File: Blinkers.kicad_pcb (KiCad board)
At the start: 2 copper layers, 250 x 49 mm, 219 parts, among them J1 12V, J2 A1, J3 gnd, J4 A1, J5 A1, J6 A1, J7 A1, J8 A1, J9 brake, Q1 Q_NMOS_DGS, Q2 Q_NMOS_DGS, Q3 Q_NMOS_DGS, Q4 Q_NMOS_DGS, Q5 Q_NMOS_DGS, Q6 Q_NMOS_DGS

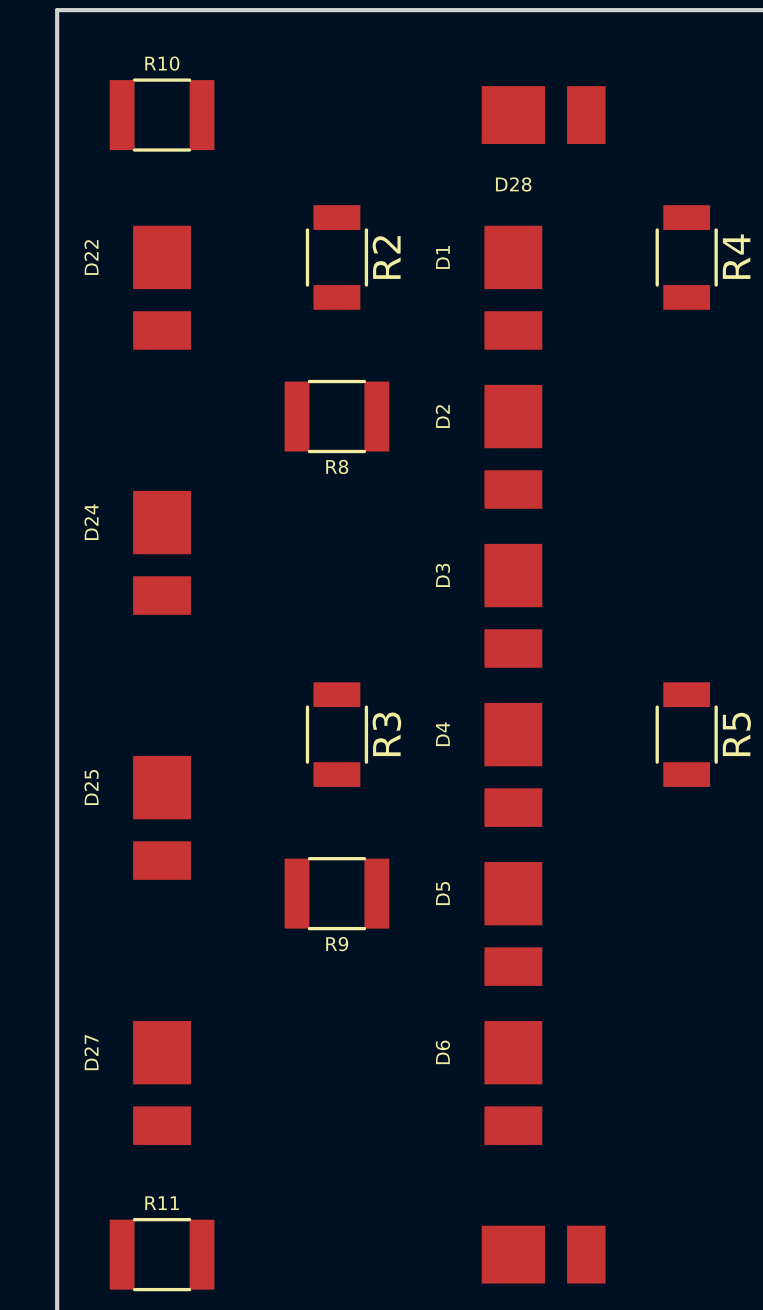
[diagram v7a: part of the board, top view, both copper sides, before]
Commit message: Fine-tuning WIP, rotating LEDs for closer connectons and moved VCC and GND.
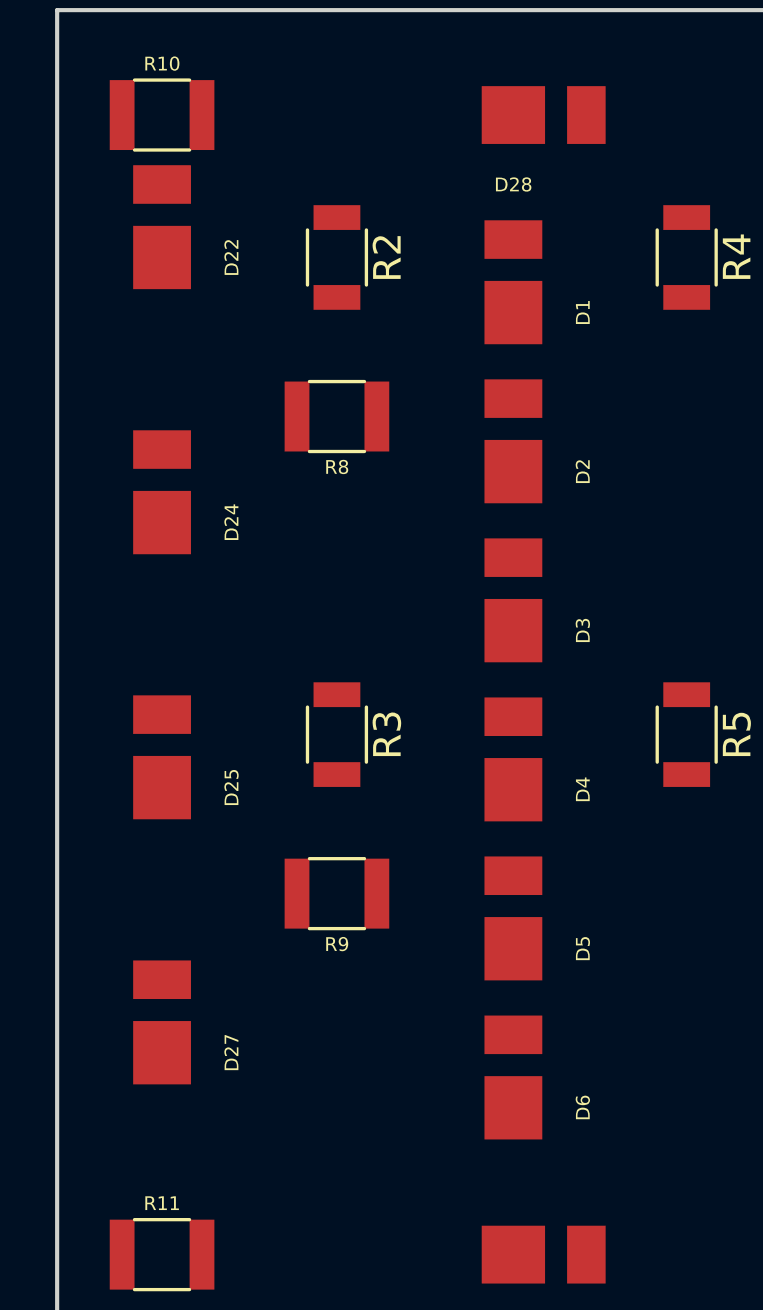
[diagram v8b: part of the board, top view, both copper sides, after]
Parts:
- moved D1 2.00 mm to (30.5, 92.3), turned to 90 degrees
- moved D2 2.00 mm to (30.5, 98.0), turned to 90 degrees
- moved D3 2.00 mm to (30.5, 103.8), turned to 90 degrees
- moved D4 2.00 mm to (30.5, 109.6), turned to 90 degrees
- moved D5 2.00 mm to (30.5, 115.4), turned to 90 degrees
- moved D6 2.00 mm to (30.5, 121.1), turned to 90 degrees
- turned D22 to 90 degrees
- turned D24 to 90 degrees
- turned D25 to 90 degrees
- turned D27 to 90 degrees
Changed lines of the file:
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@@
-(kicad_pcb (version 20171130) (host pcbnew 5.1.3-ffb9f22~84~ubuntu18.04.1)
+(kicad_pcb (version 20171130) (host pcbnew "(5.1.2)-2")
   (general
     (thickness 1.6)
@@
   )
   (module Footprints:D_2835 placed (layer F.Cu)
-    (at 17.78 90.2625 270)
+    (at 17.78 90.2625 90)
     (attr smd)
     (fp_text reference D22 (at 0 2.54 270) (layer F.SilkS)
@@
       (effects (font (size 0.5 0.5) (thickness 0.0625)))
     )
-    (pad 1 smd rect (at 0 0 270) (size 2.3 2.1) (layers F.Cu F.Paste F.Mask)
+    (pad 1 smd rect (at 0 0 90) (size 2.3 2.1) (layers F.Cu F.Paste F.Mask)
       (net 7 "Net-(D22-Pad1)"))
-    (pad 2 smd rect (at 2.65 0 270) (size 1.4 2.1) (layers F.Cu F.Paste F.Mask)
+    (pad 2 smd rect (at 2.65 0 90) (size 1.4 2.1) (layers F.Cu F.Paste F.Mask)
       (net 8 "Net-(D22-Pad2)"))
   )
   (module Footprints:D_2835 placed (layer F.Cu)
-    (at 17.78 99.8875 270)
+    (at 17.78 99.8875 90)
     (attr smd)
     (fp_text reference D24 (at 0 2.54 270) (layer F.SilkS)
@@
       (effects (font (size 0.5 0.5) (thickness 0.0625)))
     )
-    (pad 1 smd rect (at 0 0 270) (size 2.3 2.1) (layers F.Cu F.Paste F.Mask)
+    (pad 1 smd rect (at 0 0 90) (size 2.3 2.1) (layers F.Cu F.Paste F.Mask)
       (net 4 GND))
-    (pad 2 smd rect (at 2.65 0 270) (size 1.4 2.1) (layers F.Cu F.Paste F.Mask)
+    (pad 2 smd rect (at 2.65 0 90) (size 1.4 2.1) (layers F.Cu F.Paste F.Mask)
       (net 7 "Net-(D22-Pad1)"))
   )
   (module Footprints:D_2835 placed (layer F.Cu)
-    (at 17.78 109.512 270)
+    (at 17.78 109.512 90)
     (attr smd)
     (fp_text reference D25 (at 0 2.54 270) (layer F.SilkS)
@@
       (effects (font (size 0.5 0.5) (thickness 0.0625)))
     )
-    (pad 1 smd rect (at 0 0 270) (size 2.3 2.1) (layers F.Cu F.Paste F.Mask)
+    (pad 1 smd rect (at 0 0 90) (size 2.3 2.1) (layers F.Cu F.Paste F.Mask)
       (net 9 "Net-(D25-Pad1)"))
-    (pad 2 smd rect (at 2.65 0 270) (size 1.4 2.1) (layers F.Cu F.Paste F.Mask)
+    (pad 2 smd rect (at 2.65 0 90) (size 1.4 2.1) (layers F.Cu F.Paste F.Mask)
       (net 10 "Net-(D25-Pad2)"))
   )
   (module Footprints:D_2835 locked placed (layer F.Cu)
-    (at 17.78 119.138 270)
+    (at 17.78 119.138 90)
     (attr smd)
     (fp_text reference D27 (at 0 2.54 270) (layer F.SilkS)
@@
       (effects (font (size 0.5 0.5) (thickness 0.0625)))
     )
-    (pad 1 smd rect (at 0 0 270) (size 2.3 2.1) (layers F.Cu F.Paste F.Mask)
+    (pad 1 smd rect (at 0 0 90) (size 2.3 2.1) (layers F.Cu F.Paste F.Mask)
       (net 4 GND))
-    (pad 2 smd rect (at 2.65 0 270) (size 1.4 2.1) (layers F.Cu F.Paste F.Mask)
+    (pad 2 smd rect (at 2.65 0 90) (size 1.4 2.1) (layers F.Cu F.Paste F.Mask)
       (net 9 "Net-(D25-Pad1)"))
   )
@@
       (net 3 "Net-(D10-Pad1)"))
   )
-  (module Footprints:D_2835 locked placed (layer F.Cu)
-    (at 30.537 119.138 270)
+  (module Footprints:D_2835 placed (layer F.Cu)
+    (at 30.537 121.138 90)
     (attr smd)
     (fp_text reference D6 (at 0 2.54 270) (layer F.SilkS)
@@
       (effects (font (size 0.5 0.5) (thickness 0.0625)))
     )
-    (pad 1 smd rect (at 0 0 270) (size 2.3 2.1) (layers F.Cu F.Paste F.Mask)
+    (pad 1 smd rect (at 0 0 90) (size 2.3 2.1) (layers F.Cu F.Paste F.Mask)
       (net 3 "Net-(D10-Pad1)"))
-    (pad 2 smd rect (at 2.65 0 270) (size 1.4 2.1) (layers F.Cu F.Paste F.Mask)
+    (pad 2 smd rect (at 2.65 0 90) (size 1.4 2.1) (layers F.Cu F.Paste F.Mask)
       (net 64 "Net-(D5-Pad1)"))
   )
@@
       (net 70 "Net-(D12-Pad1)"))
   )
-  (module Footprints:D_2835 locked placed (layer F.Cu)
-    (at 30.537 113.362 270)
+  (module Footprints:D_2835 placed (layer F.Cu)
+    (at 30.537 115.362 90)
     (attr smd)
     (fp_text reference D5 (at 0 2.54 270) (layer F.SilkS)
@@
       (effects (font (size 0.5 0.5) (thickness 0.0625)))
     )
-    (pad 1 smd rect (at 0 0 270) (size 2.3 2.1) (layers F.Cu F.Paste F.Mask)
+    (pad 1 smd rect (at 0 0 90) (size 2.3 2.1) (layers F.Cu F.Paste F.Mask)
       (net 64 "Net-(D5-Pad1)"))
-    (pad 2 smd rect (at 2.65 0 270) (size 1.4 2.1) (layers F.Cu F.Paste F.Mask)
+    (pad 2 smd rect (at 2.65 0 90) (size 1.4 2.1) (layers F.Cu F.Paste F.Mask)
       (net 63 "Net-(D4-Pad1)"))
   )
@@
   )
   (module Footprints:D_2835 placed (layer F.Cu)
-    (at 30.537 107.588 270)
+    (at 30.537 109.588 90)
     (attr smd)
     (fp_text reference D4 (at 0 2.54 270) (layer F.SilkS)
@@
       (effects (font (size 0.5 0.5) (thickness 0.0625)))
     )
-    (pad 2 smd rect (at 2.65 0 270) (size 1.4 2.1) (layers F.Cu F.Paste F.Mask)
+    (pad 2 smd rect (at 2.65 0 90) (size 1.4 2.1) (layers F.Cu F.Paste F.Mask)
       (net 62 "Net-(D4-Pad2)"))
-    (pad 1 smd rect (at 0 0 270) (size 2.3 2.1) (layers F.Cu F.Paste F.Mask)
+    (pad 1 smd rect (at 0 0 90) (size 2.3 2.1) (layers F.Cu F.Paste F.Mask)
       (net 63 "Net-(D4-Pad1)"))
   )
@@
   )
   (module Footprints:D_2835 placed (layer F.Cu)
-    (at 30.537 101.812 270)
+    (at 30.537 103.812 90)
     (attr smd)
     (fp_text reference D3 (at 0 2.54 270) (layer F.SilkS)
@@
       (effects (font (size 0.5 0.5) (thickness 0.0625)))
     )
-    (pad 2 smd rect (at 2.65 0 270) (size 1.4 2.1) (layers F.Cu F.Paste F.Mask)
+    (pad 2 smd rect (at 2.65 0 90) (size 1.4 2.1) (layers F.Cu F.Paste F.Mask)
       (net 61 "Net-(D2-Pad1)"))
-    (pad 1 smd rect (at 0 0 270) (size 2.3 2.1) (layers F.Cu F.Paste F.Mask)
+    (pad 1 smd rect (at 0 0 90) (size 2.3 2.1) (layers F.Cu F.Paste F.Mask)
       (net 3 "Net-(D10-Pad1)"))
   )
@@
   )
   (module Footprints:D_2835 placed (layer F.Cu)
-    (at 30.537 96.0375 270)
+    (at 30.537 98.0375 90)
     (attr smd)
     (fp_text reference D2 (at 0 2.54 270) (layer F.SilkS)
@@
       (effects (font (size 0.5 0.5) (thickness 0.0625)))
     )
-    (pad 2 smd rect (at 2.65 0 270) (size 1.4 2.1) (layers F.Cu F.Paste F.Mask)
+    (pad 2 smd rect (at 2.65 0 90) (size 1.4 2.1) (layers F.Cu F.Paste F.Mask)
       (net 1 "Net-(D1-Pad1)"))
-    (pad 1 smd rect (at 0 0 270) (size 2.3 2.1) (layers F.Cu F.Paste F.Mask)
+    (pad 1 smd rect (at 0 0 90) (size 2.3 2.1) (layers F.Cu F.Paste F.Mask)
       (net 61 "Net-(D2-Pad1)"))
   )
@@
   )
   (module Footprints:D_2835 placed (layer F.Cu)
-    (at 30.537 90.2625 270)
+    (at 30.537 92.2625 90)
     (attr smd)
     (fp_text reference D1 (at 0 2.54 270) (layer F.SilkS)
@@
       (effects (font (size 0.5 0.5) (thickness 0.0625)))
     )
-    (pad 1 smd rect (at 0 0 270) (size 2.3 2.1) (layers F.Cu F.Paste F.Mask)
+    (pad 1 smd rect (at 0 0 90) (size 2.3 2.1) (layers F.Cu F.Paste F.Mask)
       (net 1 "Net-(D1-Pad1)"))
-    (pad 2 smd rect (at 2.65 0 270) (size 1.4 2.1) (layers F.Cu F.Paste F.Mask)
+    (pad 2 smd rect (at 2.65 0 90) (size 1.4 2.1) (layers F.Cu F.Paste F.Mask)
       (net 2 "Net-(D1-Pad2)"))
   )
